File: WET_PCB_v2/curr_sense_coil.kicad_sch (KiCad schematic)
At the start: 0 parts

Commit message: before i prob fuck up everything bc clearance
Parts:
- added D33, D34: D_Zener, Diode_THT:D_DO-15_P2.54mm_Vertical_CathodeUp, symbol Device:D_Zener
- added J22: LA55_GND, Connector_PinSocket_2.54mm:PinSocket_1x01_P2.54mm_Horizontal, symbol Connector:Conn_01x01_Socket
- added J23: LA55_M, Connector_PinSocket_2.54mm:PinSocket_1x01_P2.54mm_Horizontal, symbol Connector:Conn_01x01_Socket
- added J24: LA55_+, Connector_PinSocket_2.54mm:PinSocket_1x01_P2.54mm_Horizontal, symbol Connector:Conn_01x01_Socket
- added J25: Capacitor connector, Connector_PinSocket_2.54mm:PinSocket_1x02_P2.54mm_Vertical, symbol Connector_Generic:Conn_02x01
- added R46, R47: R, Resistor_SMD:R_0805_2012Metric_Pad1.20x1.40mm_HandSolder, symbol Device:R
- added U5: LA55-P, Sensor_Current:LEM_LA25-P, symbol Sensor_Current:LA55-P
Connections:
- new net: J23.1 (Pin_1), R46.1
- new net GND: D34.2 (A), J22.1 (Pin_1), J25.1 (Pin_1), R47.1
- new net VDD_clippingdiode: D33.1 (K)
- new net transducer_out_scaled: D33.2 (A), D34.1 (K), J25.2 (Pin_2), R46.2, R47.2
- new net transducer_power: J24.1 (Pin_1)
- no-connect marks 0 -> 3
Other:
- note removed: "design circuit for current sensor"

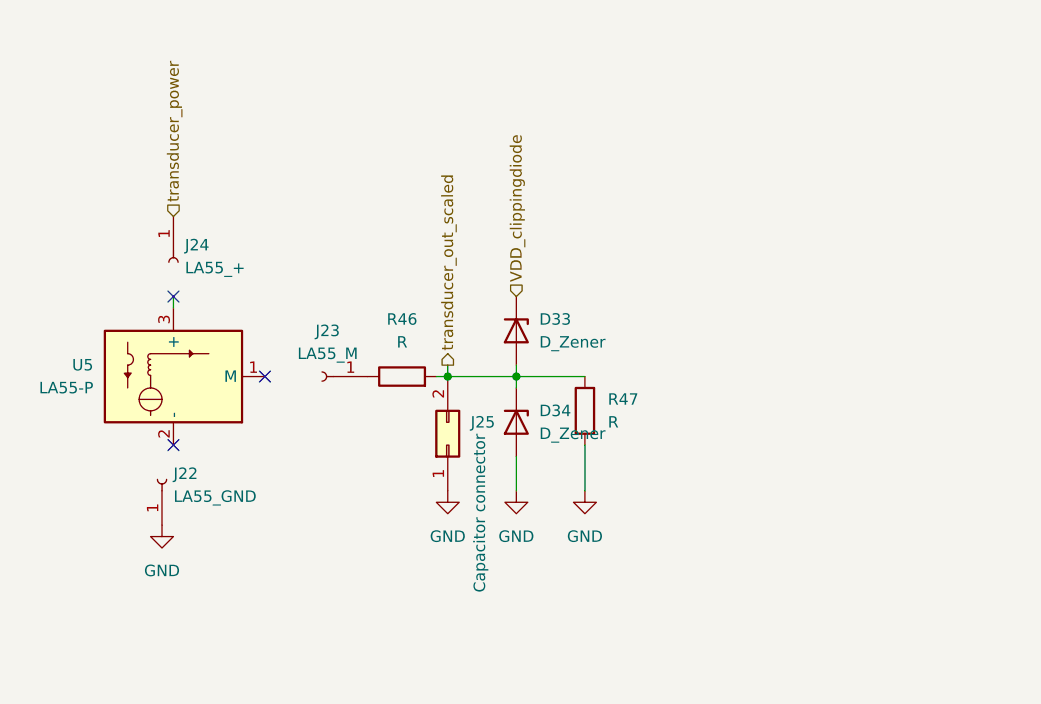
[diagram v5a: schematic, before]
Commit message: microcontroller to chip traces done
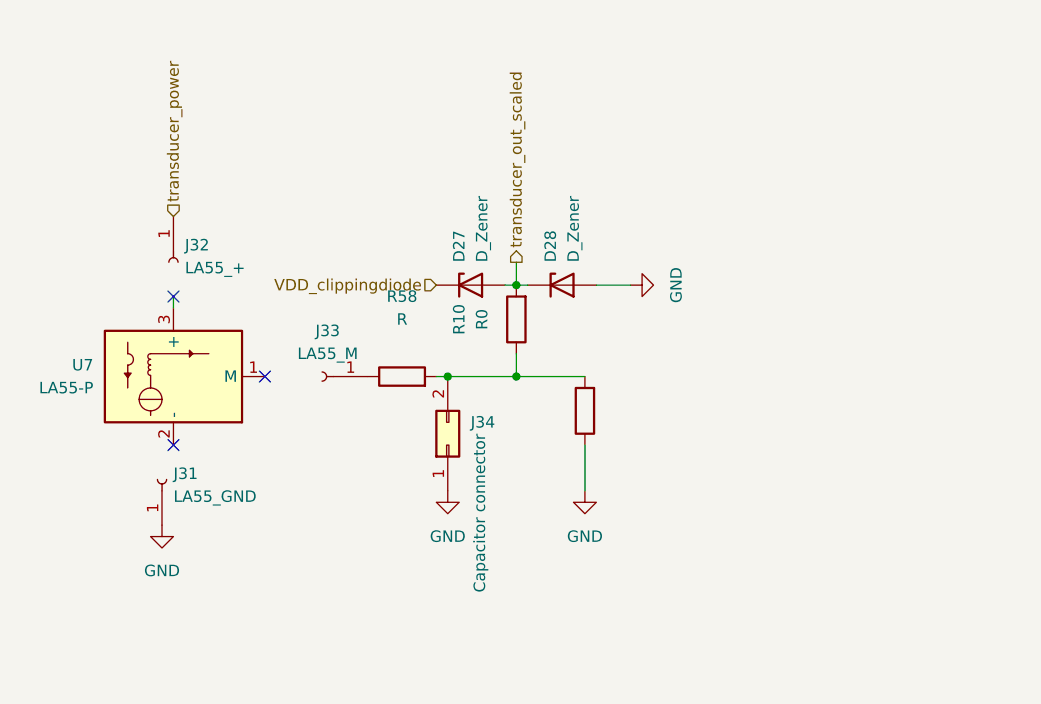
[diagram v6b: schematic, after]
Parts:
- removed D33, D34: D_Zener, Diode_THT:D_DO-15_P2.54mm_Vertical_CathodeUp, symbol Device:D_Zener
- added D27, D28: D_Zener, Diode_SMD:D_SMF, symbol Device:D_Zener
- added R10: R0, Resistor_SMD:R_0805_2012Metric_Pad1.20x1.40mm_HandSolder, symbol Device:R
- J34: renamed from J25; footprint Connector_PinSocket_2.54mm:PinSocket_1x02_P2.54mm_Vertical -> Connector_PinSocket_2.54mm:PinSocket_1x02_P2.54mm_Horizontal
- renumbered J22 to J31, J24 to J32, J23 to J33, R46 to R58, R47 to R59, U5 to U7
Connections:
- net GND: now also D28.2 (A)
- net VDD_clippingdiode: now also D27.1 (K)
- net transducer_out_scaled: now also D27.2 (A), D28.1 (K), R10.2; no longer J34.2 (Pin_2), R58.2, R59.2
- new net: J34.2 (Pin_2), R10.1, R58.2, R59.2

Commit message: labels
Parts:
- renumbered R10 to JMP24
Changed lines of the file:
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@@
 		(dnp no)
 		(fields_autoplaced yes)
-		(property "Reference" "R10"
+		(property "Reference" "JMP24"
 			(at 73.66 35.56 90)
 			(show_name no)
@@
 			(project "WET_PCB_v2"
 				(path "/13451c35-1666-47d9-9525-8d8125ba1cf3/cd9866f5-282f-4ec9-8a79-0dbe530bc090"
-					(reference "R10")
+					(reference "JMP24")
 					(unit 1)
 				)

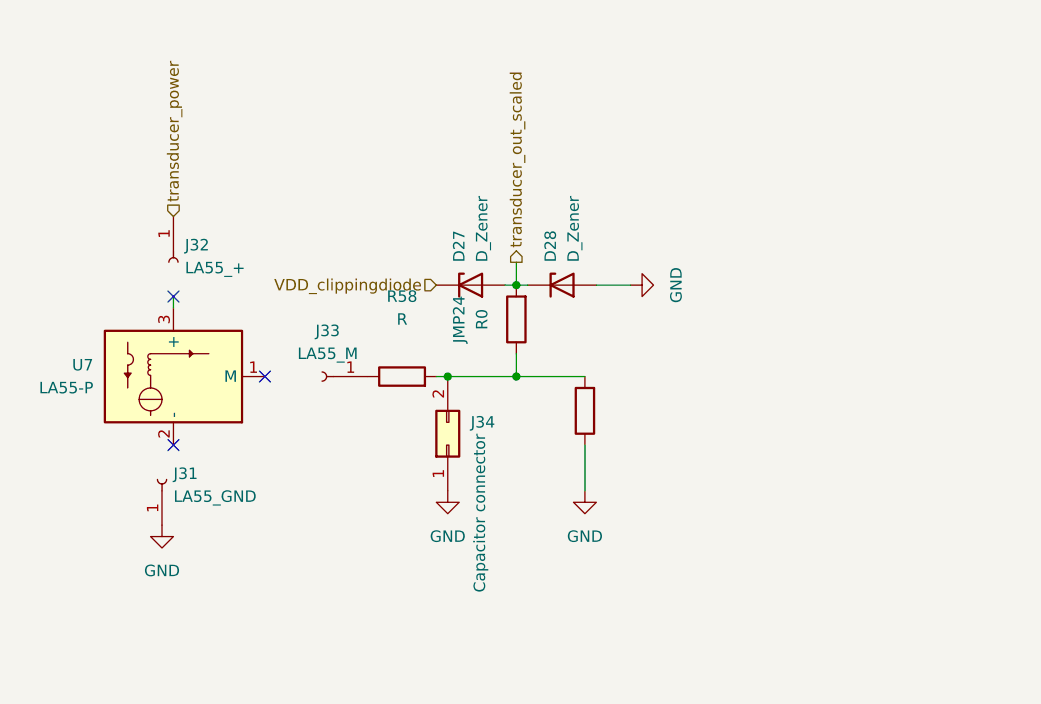
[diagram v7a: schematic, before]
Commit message: added values and notes for assembly
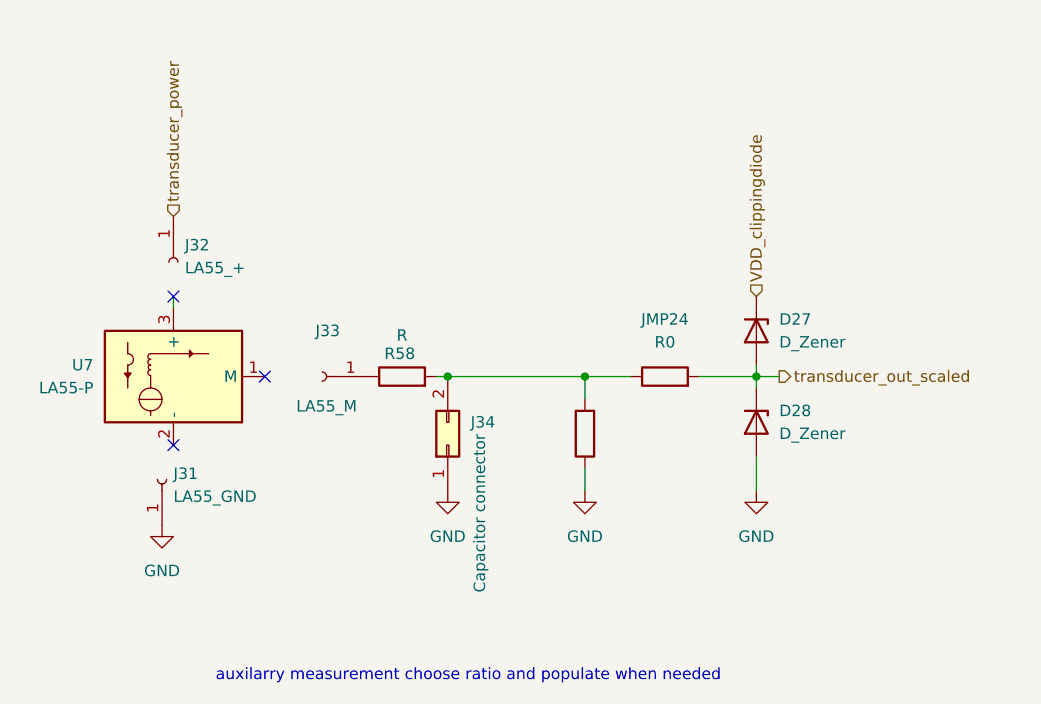
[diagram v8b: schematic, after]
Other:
- note added: "auxilarry measurement choose ratio and populate when needed"
- moved on the sheet: D27, D28, JMP24
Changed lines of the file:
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@@
 	(generator_version "10.0")
 	(paper "A4")
+	(text "auxilarry measurement choose ratio and populate when needed"
+		(exclude_from_sim no)
+		(at 74.676 75.184 0)
+		(effects
+			(font
+				(size 1.27 1.27)
+			)
+		)
+	)
+	(junction
+		(at 87.63 41.91)
+		(diameter 0)
+		(color 0 0 0 0)
+	)
 	(junction
 		(at 72.39 41.91)
@@
 	)
 	(junction
-		(at 80.01 31.75)
+		(at 106.68 41.91)
 		(diameter 0)
 		(color 0 0 0 0)
 	)
-	(junction
-		(at 80.01 41.91)
-		(diameter 0)
-		(color 0 0 0 0)
-	)
 	(no_connect
 		(at 41.91 33.02)
@@
 	(wire
 		(pts
-			(xy 80.01 29.21) (xy 80.01 31.75)
+			(xy 100.33 41.91) (xy 106.68 41.91)
 		)
 		(stroke
@@
 	(wire
 		(pts
-			(xy 92.71 31.75) (xy 88.9 31.75)
+			(xy 109.22 41.91) (xy 106.68 41.91)
 		)
 		(stroke
@@
 	(wire
 		(pts
-			(xy 72.39 41.91) (xy 80.01 41.91)
+			(xy 106.68 54.61) (xy 106.68 50.8)
 		)
 		(stroke
@@
 	(wire
 		(pts
-			(xy 80.01 41.91) (xy 87.63 41.91)
+			(xy 87.63 44.45) (xy 87.63 41.91)
 		)
 		(stroke
@@
 	(wire
 		(pts
-			(xy 41.91 33.02) (xy 41.91 34.29)
+			(xy 72.39 41.91) (xy 87.63 41.91)
 		)
 		(stroke
@@
 	(wire
 		(pts
-			(xy 78.74 31.75) (xy 80.01 31.75)
+			(xy 41.91 33.02) (xy 41.91 34.29)
 		)
 		(stroke
@@
 	(wire
 		(pts
-			(xy 87.63 54.61) (xy 87.63 49.53)
+			(xy 106.68 40.64) (xy 106.68 41.91)
 		)
 		(stroke
@@
 	(wire
 		(pts
-			(xy 80.01 39.37) (xy 80.01 41.91)
+			(xy 87.63 54.61) (xy 87.63 52.07)
 		)
 		(stroke
@@
 	(wire
 		(pts
-			(xy 80.01 31.75) (xy 81.28 31.75)
+			(xy 92.71 41.91) (xy 87.63 41.91)
+		)
+		(stroke
+			(width 0)
+			(type default)
+		)
+	)
+	(wire
+		(pts
+			(xy 106.68 41.91) (xy 106.68 43.18)
 		)
 		(stroke
@@
 	(hierarchical_label "transducer_out_scaled"
 		(shape output)
-		(at 80.01 29.21 90)
+		(at 109.22 41.91 0)
 		(effects
 			(font
@@
 	(hierarchical_label "VDD_clippingdiode"
 		(shape input)
-		(at 71.12 31.75 180)
+		(at 106.68 33.02 90)
 		(effects
 			(font
 				(size 1.27 1.27)
 			)
-			(justify right)
+			(justify left)
 		)
 	)
@@
 	(symbol
 		(lib_id "power:GND")
-		(at 92.71 31.75 90)
+		(at 106.68 54.61 0)
 		(unit 1)
 		(body_style 1)
@@
 		(fields_autoplaced yes)
 		(property "Reference" "#PWR065"
-			(at 99.06 31.75 0)
+			(at 106.68 60.96 0)
 			(hide yes)
 			(show_name no)
@@
 		)
 		(property "Value" "GND"
-			(at 97.79 31.75 0)
+			(at 106.68 59.69 0)
 			(show_name no)
 			(do_not_autoplace no)
@@
 		)
 		(property "Footprint" ""
-			(at 92.71 31.75 0)
+			(at 106.68 54.61 0)
 			(hide yes)
 			(show_name no)
@@
 		)
 		(property "Datasheet" ""
-			(at 92.71 31.75 0)
+			(at 106.68 54.61 0)
 			(hide yes)
 			(show_name no)
@@
 		)
 		(property "Description" "Power symbol creates a global label with name \"GND\" , ground"
-			(at 92.71 31.75 0)
+			(at 106.68 54.61 0)
 			(hide yes)
 			(show_name no)
@@
 		(in_pos_files yes)
 		(dnp no)
-		(fields_autoplaced yes)
 		(property "Reference" "J33"
 			(at 59.055 36.83 0)
@@
 		)
 		(property "Value" "LA55_M"
-			(at 59.055 39.37 0)
+			(at 58.928 45.212 0)
 			(show_name no)
 			(do_not_autoplace no)
@@
 	(symbol
 		(lib_id "Device:D_Zener")
-		(at 85.09 31.75 0)
+		(at 106.68 46.99 270)
 		(unit 1)
 		(body_style 1)
@@
 		(fields_autoplaced yes)
 		(property "Reference" "D28"
-			(at 83.8199 29.21 90)
+			(at 109.22 45.7199 90)
 			(show_name no)
 			(do_not_autoplace no)
@@
 		)
 		(property "Value" "D_Zener"
-			(at 86.3599 29.21 90)
+			(at 109.22 48.2599 90)
 			(show_name no)
 			(do_not_autoplace no)
@@
 		)
 		(property "Footprint" "Diode_SMD:D_SMF"
-			(at 85.09 31.75 0)
+			(at 106.68 46.99 0)
 			(hide yes)
 			(show_name no)
@@
 		)
 		(property "Datasheet" ""
-			(at 85.09 31.75 0)
+			(at 106.68 46.99 0)
 			(hide yes)
 			(show_name no)
@@
 		)
 		(property "Description" "Zener diode"
-			(at 85.09 31.75 0)
+			(at 106.68 46.99 0)
 			(hide yes)
 			(show_name no)
@@
 	(symbol
 		(lib_id "Device:D_Zener")
-		(at 74.93 31.75 0)
+		(at 106.68 36.83 270)
 		(unit 1)
 		(body_style 1)
@@
 		(fields_autoplaced yes)
 		(property "Reference" "D27"
-			(at 73.6599 29.21 90)
+			(at 109.22 35.5599 90)
 			(show_name no)
 			(do_not_autoplace no)
@@
 		)
 		(property "Value" "D_Zener"
-			(at 76.1999 29.21 90)
+			(at 109.22 38.0999 90)
 			(show_name no)
 			(do_not_autoplace no)
@@
 		)
 		(property "Footprint" "Diode_SMD:D_SMF"
-			(at 74.93 31.75 0)
+			(at 106.68 36.83 0)
 			(hide yes)
 			(show_name no)
@@
 		)
 		(property "Datasheet" ""
-			(at 74.93 31.75 0)
+			(at 106.68 36.83 0)
 			(hide yes)
 			(show_name no)
@@
 		)
 		(property "Description" "Zener diode"
-			(at 74.93 31.75 0)
+			(at 106.68 36.83 0)
 			(hide yes)
 			(show_name no)
@@
 	(symbol
 		(lib_id "Device:R")
-		(at 80.01 35.56 180)
+		(at 96.52 41.91 90)
 		(unit 1)
 		(body_style 1)
@@
 		(fields_autoplaced yes)
 		(property "Reference" "JMP24"
-			(at 73.66 35.56 90)
+			(at 96.52 35.56 90)
 			(show_name no)
 			(do_not_autoplace no)
@@
 		)
 		(property "Value" "R0"
-			(at 76.2 35.56 90)
+			(at 96.52 38.1 90)
 			(show_name no)
 			(do_not_autoplace no)
@@
 		)
 		(property "Footprint" "Resistor_SMD:R_0805_2012Metric_Pad1.20x1.40mm_HandSolder"
-			(at 81.788 35.56 90)
+			(at 96.52 43.688 90)
 			(hide yes)
 			(show_name no)
@@
 		)
 		(property "Datasheet" ""
-			(at 80.01 35.56 0)
+			(at 96.52 41.91 0)
 			(hide yes)
 			(show_name no)
@@
 		)
 		(property "Description" "Resistor"
-			(at 80.01 35.56 0)
+			(at 96.52 41.91 0)
 			(hide yes)
 			(show_name no)
@@
 		(dnp no)
 		(property "Reference" "R58"
-			(at 67.31 33.02 90)
+			(at 67.056 39.37 90)
 			(show_name no)
 			(do_not_autoplace no)
@@
 		)
 		(property "Value" "R"
-			(at 67.31 35.56 90)
+			(at 67.31 37.338 90)
 			(show_name no)
 			(do_not_autoplace no)
@@
 	(symbol
 		(lib_id "Device:R")
-		(at 87.63 45.72 180)
+		(at 87.63 48.26 180)
 		(unit 1)
 		(body_style 1)
@@
 		(fields_autoplaced yes)
 		(property "Reference" "R59"
-			(at 90.17 44.4499 0)
+			(at 90.17 46.9899 0)
 			(hide yes)
 			(show_name no)
@@
 		)
 		(property "Value" "R"
-			(at 90.17 46.9899 0)
+			(at 90.17 49.5299 0)
 			(hide yes)
 			(show_name no)
@@
 		)
 		(property "Footprint" "Resistor_SMD:R_0805_2012Metric_Pad1.20x1.40mm_HandSolder"
-			(at 89.408 45.72 90)
+			(at 89.408 48.26 90)
 			(hide yes)
 			(show_name no)
@@
 		)
 		(property "Datasheet" ""
-			(at 87.63 45.72 0)
+			(at 87.63 48.26 0)
 			(hide yes)
 			(show_name no)
@@
 		)
 		(property "Description" "Resistor"
-			(at 87.63 45.72 0)
-			(hide yes)
-			(show_name no)
+			(at 87.63 48.26 0)
+			(hide yes)
+			(show_name no)
